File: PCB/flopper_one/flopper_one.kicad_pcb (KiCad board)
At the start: 2 copper layers, 76.8 x 63 mm, 22 parts, among them J1 To PN532 ->, J2 <- ST7789, Q1 2N2219, SW1 SW_Omron_B3FS, SW2 SW_Omron_B3FS, SW3 SW_Omron_B3FS, SW4 SW_Omron_B3FS, SW5 SW_Omron_B3FS, U1 TP4056-42-ESOP8, U4 hw-045

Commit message: fix minor error
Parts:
- removed ON=DSG: SW_SPST, wroom:my_switch
- added C2: 10uf, Capacitor_THT:CP_Axial_L10.0mm_D4.5mm_P15.00mm_Horizontal, B.Cu at (190.3, 120.5)
- added SW6: SW_SPST, wroom:my_switch, F.Cu at (212.0, 118.2)
- moved C1 3.51 mm to (193.8, 87.5)
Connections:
- U1 pad 8: /VCC -> /VIN
- U4 pad 1: Net-(SW6-B) -> /VIN
- U4 pad 4: /BAT+ -> Net-(SW6-A)
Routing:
- net Net-(SW6-A): track 0.00 -> 32.0 mm
- net /VCC: track 183.9 -> 168.6 mm, vias 3 -> 1
- net /BAT+: track 31.1 -> 45.9 mm
- net /VIN: track 45.5 -> 58.7 mm
- net Net-(SW6-B): track 4.99 -> 0.00 mm
- net GND: track 347.9 -> 352.5 mm
- net /SCL2: track 62.8 -> 60.9 mm
- net /SDA2: track 57.1 -> 56.1 mm
- net Net-(U2-GPIO23): track 96.6 -> 97.3 mm

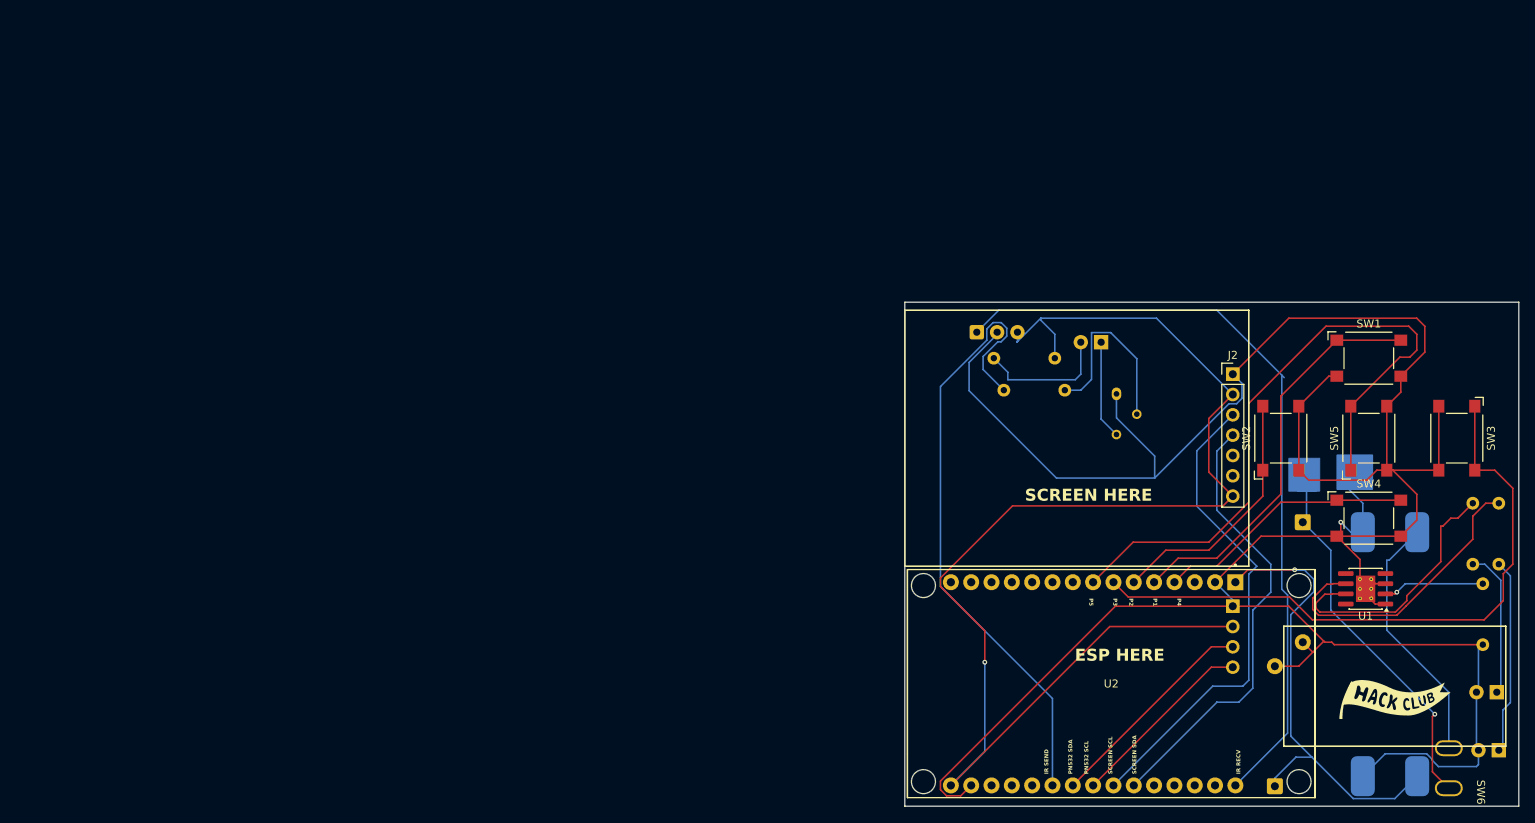
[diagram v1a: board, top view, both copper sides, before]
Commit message: move stuff around
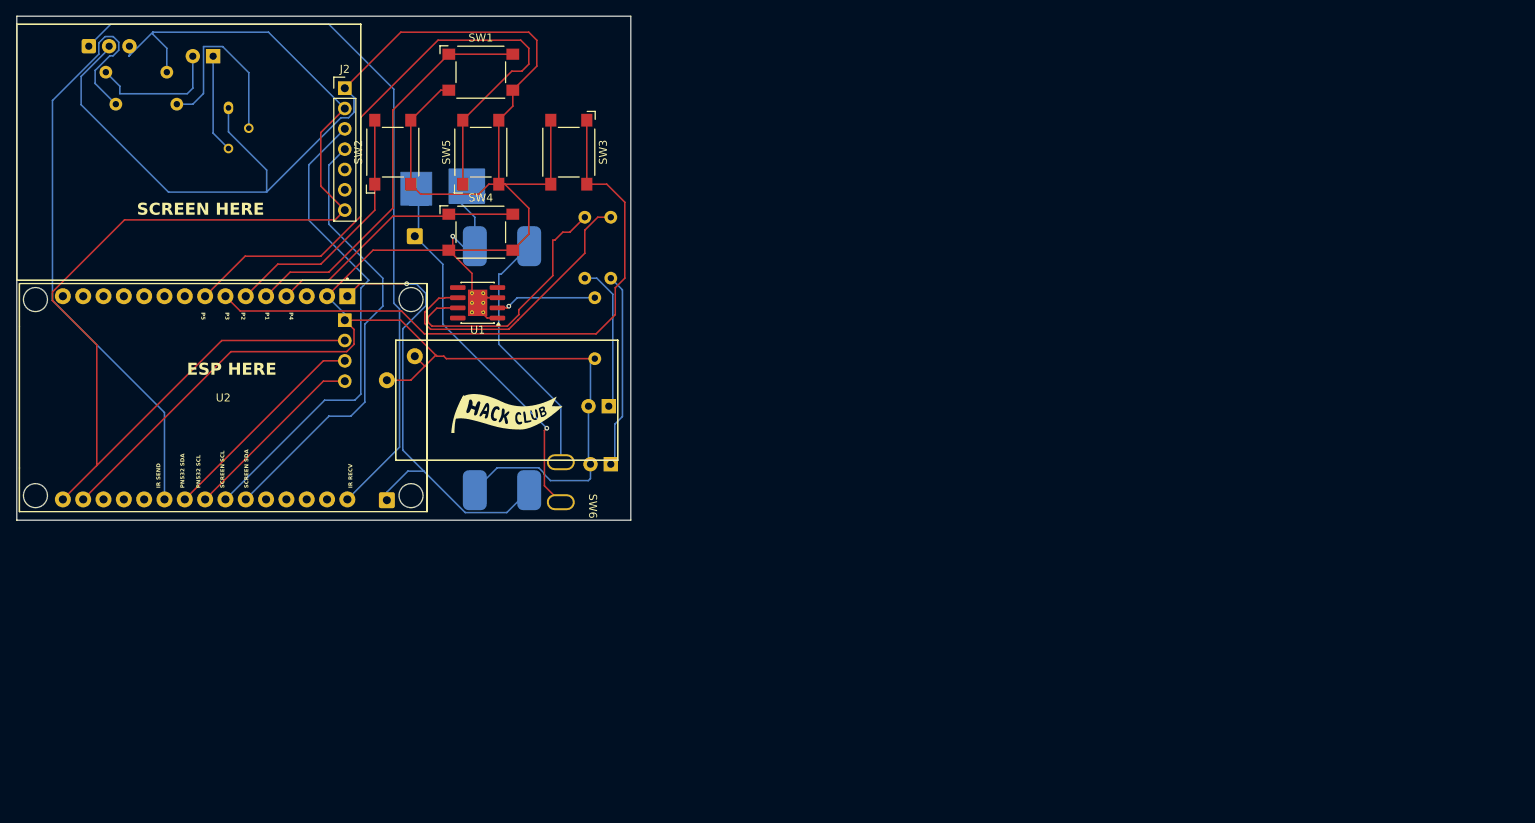
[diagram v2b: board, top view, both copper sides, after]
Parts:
- moved C1 116.6 mm to (82.8, 51.8)
- moved C2 116.6 mm to (79.3, 84.8)
- moved D1 116.6 mm to (57.5, 29.2)
- moved D2 116.6 mm to (107.0, 73.0)
- moved D3 116.6 mm to (107.2, 80.2)
- moved J1 116.6 mm to (74.0, 62.2)
- moved J2 116.6 mm to (74.0, 33.2)
- moved Q1 116.6 mm to (59.5, 35.7)
- moved R1 116.6 mm to (44.1, 31.2)
- moved R2 116.6 mm to (53.0, 35.2)
- moved R3 116.6 mm to (105.2, 59.4)
- moved R4 116.6 mm to (107.2, 49.4)
- moved R5 116.6 mm to (104.0, 49.4)
- moved SW1 116.6 mm to (91.0, 31.2)
- moved SW2 116.6 mm to (80.0, 41.2)
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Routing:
- net /VCC: track 168.6 -> 162.6 mm, vias 1 -> 0
- net GND: track 352.5 -> 346.5 mm

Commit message: uhm fix drc errors
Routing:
- net /VIN: track 58.7 -> 77.2 mm, vias 1 -> 2
- net /BAT+: track 45.9 -> 48.5 mm, vias 1 -> 2
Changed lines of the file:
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@@
 			(at -0.7 -1.2 180)
 			(size 0.5 0.5)
-			(drill 0.2)
+			(drill 0.3)
 			(property pad_prop_heatsink)
 			(layers "*.Cu")
@@
 			(at -0.7 0 180)
 			(size 0.5 0.5)
-			(drill 0.2)
+			(drill 0.3)
 			(property pad_prop_heatsink)
 			(layers "*.Cu")
@@
 			(at -0.7 1.2 180)
 			(size 0.5 0.5)
-			(drill 0.2)
+			(drill 0.3)
 			(property pad_prop_heatsink)
 			(layers "*.Cu")
@@
 			(at 0.7 -1.2 180)
 			(size 0.5 0.5)
-			(drill 0.2)
+			(drill 0.3)
 			(property pad_prop_heatsink)
 			(layers "*.Cu")
@@
 			(at 0.7 0 180)
 			(size 0.5 0.5)
-			(drill 0.2)
+			(drill 0.3)
 			(property pad_prop_heatsink)
 			(layers "*.Cu")
@@
 			(at 0.7 1.2 180)
 			(size 0.5 0.5)
-			(drill 0.2)
+			(drill 0.3)
 			(property pad_prop_heatsink)
 			(layers "*.Cu")
@@
 	)
 	(segment
+		(start 88.125 58.17)
+		(end 88.125 58.125)
+		(width 0.2)
+		(layer "F.Cu")
+		(net 39)
+	)
+	(segment
+		(start 88.125 58.125)
+		(end 87 57)
+		(width 0.2)
+		(layer "F.Cu")
+		(net 39)
+	)
+	(segment
 		(start 101 85)
 		(end 98.949 82.949)
@@
 		(net 39)
 	)
+	(via
+		(at 87 57)
+		(size 0.6)
+		(drill 0.3)
+		(layers "F.Cu" "B.Cu")
+		(net 39)
+	)
 	(segment
 		(start 83.21875 46.71875)
@@
 	)
 	(segment
+		(start 86.25 62.75)
+		(end 86.25 56.25)
+		(width 0.2)
+		(layer "B.Cu")
+		(net 39)
+	)
+	(segment
 		(start 99.25 75.75)
 		(end 86.25 62.75)
@@
 	)
 	(segment
-		(start 86.25 62.75)
+		(start 87 57)
+		(end 86.25 56.25)
+		(width 0.2)
+		(layer "B.Cu")
+		(net 39)
+	)
+	(segment
+		(start 86.25 56.25)
 		(end 86.25 55.25)
 		(width 0.2)
@@
 	)
 	(segment
+		(start 94.090968 62.581)
+		(end 88.726 62.581)
+		(width 0.2)
+		(layer "F.Cu")
+		(net 40)
+	)
+	(segment
 		(start 81.734516 57.693906)
 		(end 75.876094 57.693906)
@@
 	)
 	(segment
+		(start 94.049999 58.17)
+		(end 95.101 59.221001)
+		(width 0.2)
+		(layer "F.Cu")
+		(net 40)
+	)
+	(segment
+		(start 95.101 59.221001)
+		(end 95.101 61.570968)
+		(width 0.2)
+		(layer "F.Cu")
+		(net 40)
+	)
+	(segment
 		(start 75.876094 57.693906)
 		(end 74.32 59.25)
@@
 		(net 40)
 	)
+	(segment
+		(start 88.125 61.98)
+		(end 85.88 61.98)
+		(width 0.2)
+		(layer "F.Cu")
+		(net 40)
+	)
+	(segment
+		(start 85.88 61.98)
+		(end 85.65 61.75)
+		(width 0.2)
+		(layer "F.Cu")
+		(net 40)
+	)
+	(segment
+		(start 95.101 61.570968)
+		(end 94.090968 62.581)
+		(width 0.2)
+		(layer "F.Cu")
+		(net 40)
+	)
+	(segment
+		(start 93.075 58.17)
+		(end 94.049999 58.17)
+		(width 0.2)
+		(layer "F.Cu")
+		(net 40)
+	)
+	(segment
+		(start 88.726 62.581)
+		(end 88.125 61.98)
+		(width 0.2)
+		(layer "F.Cu")
+		(net 40)
+	)
 	(via
 		(at 81.734516 57.693906)
@@
 		(net 40)
 	)
+	(via
+		(at 85.65 61.75)
+		(size 0.6)
+		(drill 0.3)
+		(layers "F.Cu" "B.Cu")
+		(net 40)
+	)
 	(segment
 		(start 81.75 57.70939)
@@
 	)
 	(segment
+		(start 85.65 60.422291)
+		(end 84.131 58.903291)
+		(width 0.2)
+		(layer "B.Cu")
+		(net 40)
+	)
+	(segment
 		(start 83.88183 81.11817)
 		(end 89.06466 86.301)
 		(width 0.2)
 		(layer "B.Cu")
+		(net 40)
+	)
+	(segment
+		(start 85.65 61.75)
+		(end 85.65 60.422291)
+		(width 0.2)
+		(layer "B.Cu")

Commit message: shove cap again
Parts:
- moved C2 4.94 mm to (82.8, 81.2)
- moved C1 3.01 mm to (82.5, 48.8)
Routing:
- net GND: track 346.5 -> 359.1 mm, vias 1 -> 2
- net /BAT+: track 48.5 -> 60.0 mm, vias 2 -> 0
- net /VIN: track 77.2 -> 71.4 mm
- net /P4: track 32.5 -> 34.9 mm
- net /P3: track 79.9 -> 80.6 mm
- net Net-(U2-GPIO23): track 96.9 -> 96.3 mm

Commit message: yum yum clean traces
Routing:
- net GND: track 359.1 -> 355.4 mm
- net Net-(U1-~{STDBY}): track 37.3 -> 36.4 mm
- net /SCL2: track 60.9 -> 60.1 mm
- net Net-(U1-~{CHRG}): track 33.3 -> 32.6 mm
